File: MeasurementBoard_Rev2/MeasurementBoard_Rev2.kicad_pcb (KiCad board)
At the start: 4 copper layers, 76.2 x 88.9 mm, 113 parts, among them J1 Conn_02x19_Odd_Even, J10 MillMax_0914-2, J19 Conn_01x02_Pin, J2 Conn_02x19_Odd_Even, J20 Conn_01x02_Pin, J21 Conn_01x02_Pin, J22 Conn_01x02_Pin, J3 MillMax_0914-2, J4 MillMax_0914-2, J6 MIllMaxSpringConnector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

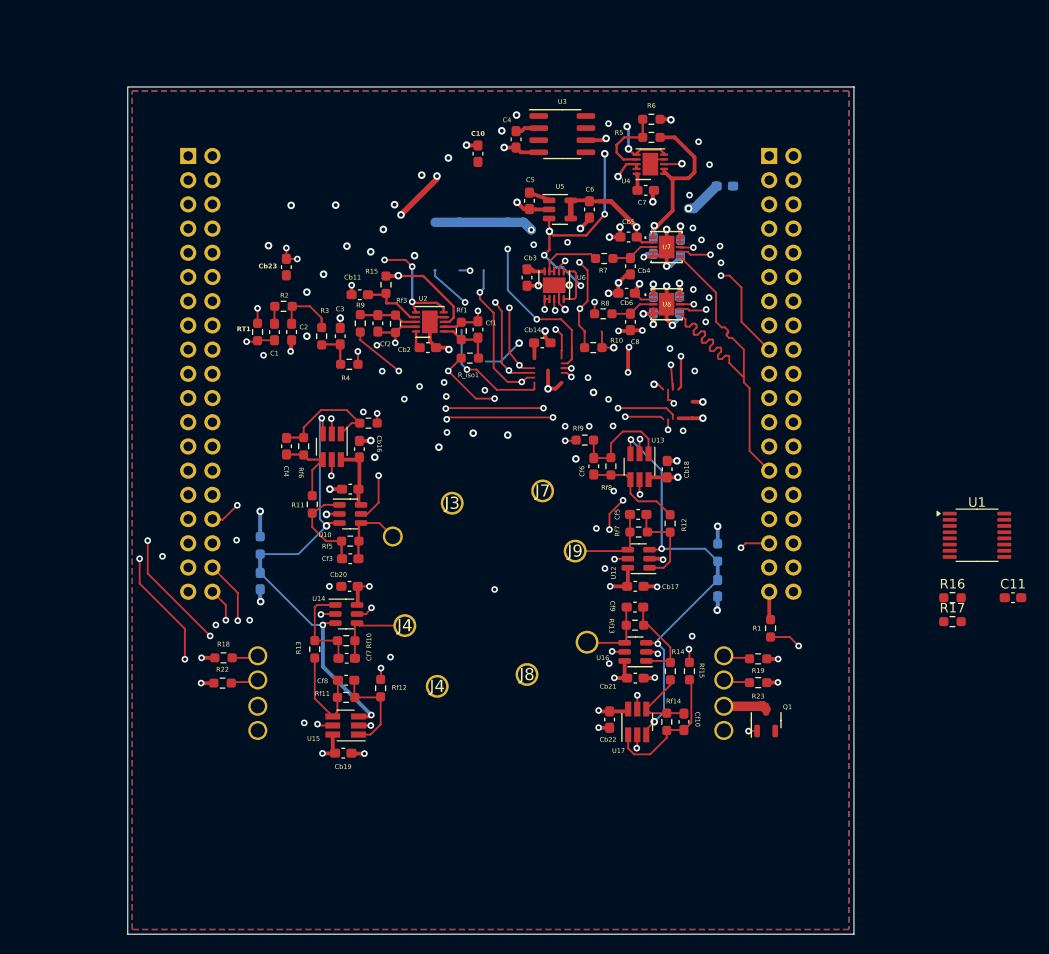
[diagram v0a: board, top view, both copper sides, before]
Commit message: Finished Measurement Board Update Minus Heater Board Connections
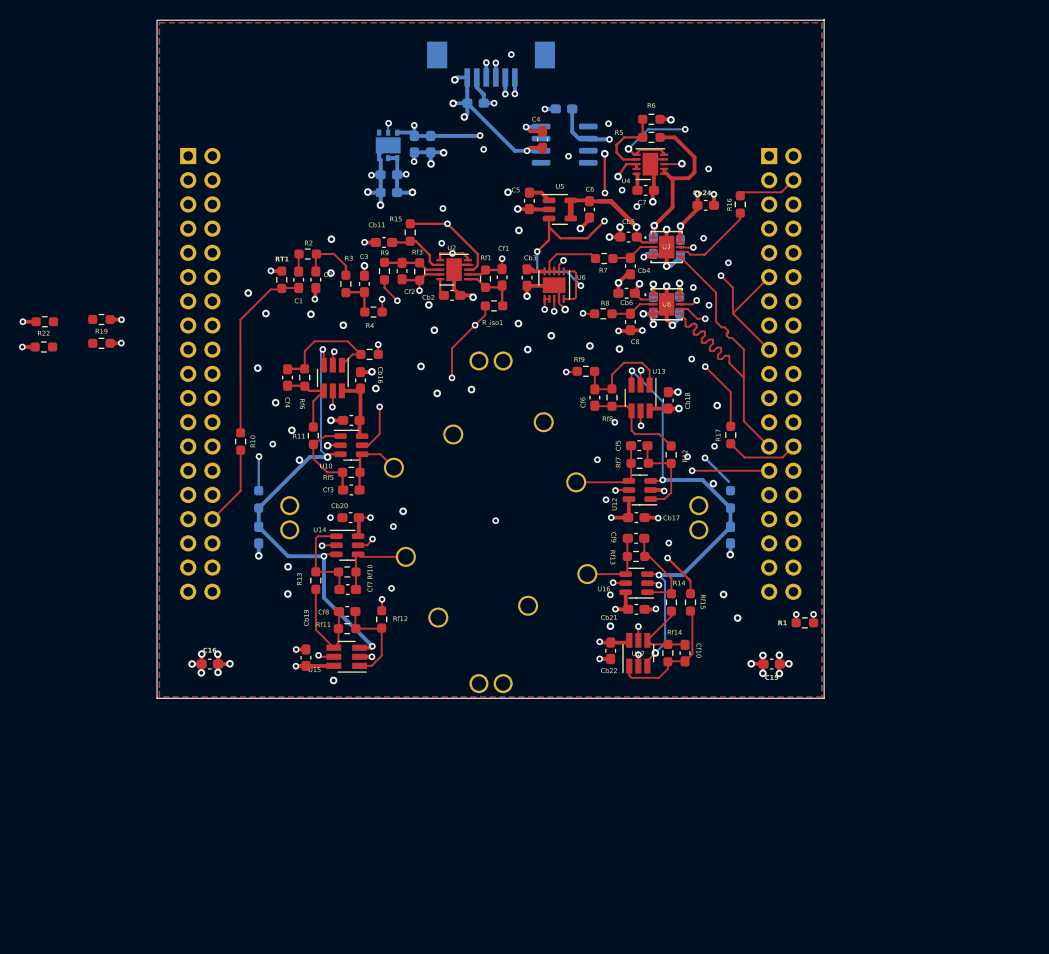
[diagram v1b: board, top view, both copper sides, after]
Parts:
- removed Cb14: 0.1u, Capacitor_SMD:C_0603_1608Metric_Pad1.08x0.95mm_HandSolder
- removed Cb23: 10u, Capacitor_SMD:C_0603_1608Metric_Pad1.08x0.95mm_HandSolder
- removed J10, J9: MillMax_0914-2, 
- removed J19, J20, J21, J22: Conn_01x02_Pin, GenIILibrary:Samtec_Pin_Socket_SS_102_G_2
- removed the J4 at (57.4, 160.9)
- removed the J4 at (54.0, 154.5)
- removed Q1: PMV30UN2, Package_TO_SOT_SMD:SOT-23-3
- removed U1: CD74AC238, Package_SO:TSSOP-16_4.4x5mm_P0.65mm
- added C12: 1uF/XR5, Capacitor_SMD:C_0603_1608Metric_Pad1.08x0.95mm_HandSolder, B.Cu at (52.3, 109.1)
- added C13: 100n, Capacitor_SMD:C_0603_1608Metric_Pad1.08x0.95mm_HandSolder, B.Cu at (55.0, 104.0)
- added C14: 100n, Capacitor_SMD:C_0603_1608Metric_Pad1.08x0.95mm_HandSolder, B.Cu at (52.3, 107.2)
- added C15: 22u, Capacitor_SMD:C_0603_1608Metric_Pad1.08x0.95mm_HandSolder, F.Cu at (92.5, 158.6)
- added C16: 22u, Capacitor_SMD:C_0603_1608Metric_Pad1.08x0.95mm_HandSolder, F.Cu at (33.5, 158.6)
- added C9: 1uF/XR5, Capacitor_SMD:C_0603_1608Metric_Pad1.08x0.95mm_HandSolder, B.Cu at (56.7, 104.0)
- added CN1: Conn_02x19_Odd_Even, Connector_PinSocket_2.54mm:PinSocket_2x19_P2.54mm_Vertical, B.Cu at (31.2, 105.2)
- added CN2: Conn_02x19_Odd_Even, Connector_PinSocket_2.54mm:PinSocket_2x19_P2.54mm_Vertical, B.Cu at (92.2, 105.2)
- added CN3: 52271-0679, GenIILibrary:MOLEX_52271-0679, B.Cu at (63.0, 93.5)
- added CN4: Conn_01x02_Pin, GenIILibrary:Samtec_Pin_Socket_SS_102_G_2, F.Cu at (41.9, 143.2)
- added CN5: Conn_01x02_Pin, GenIILibrary:Samtec_Pin_Socket_SS_102_G_2, F.Cu at (84.8, 143.2)
- added CN6: Conn_01x02_Pin, GenIILibrary:Samtec_Pin_Socket_SS_102_G_2, F.Cu at (63.0, 126.8)
- added CN7: Conn_01x02_Pin, GenIILibrary:Samtec_Pin_Socket_SS_102_G_2, F.Cu at (63.0, 160.6)
- added J4: MIllMaxSpringConnector, TCGenI_Rev3_Redo:MillMax_0914-2, F.Cu at (57.5, 153.7)
- added J5: MIllMaxSpringConnector, TCGenI_Rev3_Redo:MillMax_0914-2, F.Cu at (72.5, 138.1)
- added U9: LD39200_Fixed, Package_DFN_QFN:DFN-6-1EP_3x3mm_P0.95mm_EP1.7x2.6mm, B.Cu at (52.2, 104.1)
- C10, C11, U3: moved to B.Cu
- Cb24: moved to F.Cu
- J1, J2: value Conn_02x19_Odd_Even -> MIllMaxSpringConnector; footprint Connector_PinSocket_2.54mm:PinSocket_2x19_P2.54mm_Vertical -> TCGenI_Rev3_Redo:MillMax_0914-2; moved to F.Cu
- J3, J7, J8: value MillMax_0914-2 -> MIllMaxSpringConnector; footprint (none) -> TCGenI_Rev3_Redo:MillMax_0914-2
- R1: value 10k -> 33
- moved R19 77.6 mm to (22.1, 122.4)
- moved R23 77.6 mm to (22.1, 124.9)
- moved C11 69.6 mm to (70.7, 100.3)
- moved J1 59.6 mm to (73.0, 147.8), turned to 0 degrees
- moved J2 55.2 mm to (55.0, 146.0), turned to 0 degrees
- moved R16 46.9 mm to (89.2, 110.3), turned to 90 degrees
- moved R22 39.9 mm to (16.1, 125.3)
- moved R18 39.9 mm to (16.2, 122.6)
- moved R10 38.3 mm to (36.8, 135.2), turned to 90 degrees
- moved R17 30.4 mm to (88.2, 134.5), turned to 90 degrees
- moved Cb19 10.7 mm to (43.6, 157.9), turned to -90 degrees
- moved J6 9.13 mm to (53.8, 136.1)
- moved J8 8.84 mm to (66.9, 150.8)
- moved Rf9 7.21 mm to (73.0, 127.8)
- moved Cb17 7.21 mm to (78.3, 143.2)
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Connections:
- net /ABBCore_Alt/~{TIA1_SHDN} renamed ~{TIA1_SHDN}
- net /ABBCore_Alt/~{TIA2_SHDN} renamed ~{TIA2_SHDN}
- net /ABBCore_Alt/~{TIA3_SHDN} renamed ~{TIA3_SHDN}
- net /ABBCore_Alt/~{TIA4_SHDN} renamed ~{TIA4_SHDN}
- Cb10 pad 2: Vdd_MCU -> Vdd_Main
- Cb24 pad 2: Vdd_MCU -> Vdd_Main
- Cb9 pad 2: Vdd_MCU -> Vdd_Main
- J1 pad 1: unconnected-(J1-Pin_1-Pad1) -> CCOut_4
- J2 pad 1: unconnected-(J2-Pin_1-Pad1) -> CCOut_3
- R1 pad 1: Net-(Q1-G) -> /MCU Connections/PB6
- R1 pad 2: Heater_PWM -> UART_TX
- R16 pad 2: /MCU Connections/PA6 -> /MCU Connections/PB4
- R17 pad 1: /MCU Connections/PA7 -> /MCU Connections/PB15
- U2 pad 5: ~{CC_Drive_SHDN} -> ~{ADC1_SHDN}
- U2 pad 6: ~{CC_Drive_SHDN} -> ~{ADC1_SHDN}
- U7 pad 10: Vdd_MCU -> Vdd_Main
- U7 pad 9: Vdd_MCU -> Vdd_Main
- U8 pad 10: Vdd_MCU -> Vdd_Main
- U8 pad 9: Vdd_MCU -> Vdd_Main
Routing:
- net /ABBCore_Alt/V_Resp: track 224.5 -> 95.0 mm, vias 19 -> 5
- net UART_TX: track 0.00 -> 92.2 mm, vias 0 -> 2
- net Vdd_MCU: track 72.1 -> 0.00 mm, vias 3 -> 0
- net UART_RX: track 0.00 -> 45.0 mm, vias 0 -> 1
- net ~{CC_Drive_SHDN}: track 34.4 -> 0.00 mm, vias 3 -> 0
- net ~{TIA3_SHDN}: track 65.9 -> 32.1 mm, vias 5 -> 2
- net Vdd_Main: track 48.2 -> 79.8 mm, vias 29 -> 53
- net D1: track 28.3 -> 0.00 mm, vias 2 -> 0
- net D0: track 28.1 -> 0.00 mm, vias 2 -> 0
- net V_MID: track 144.1 -> 117.0 mm, vias 8 -> 4
- net 5V: track 26.9 -> 0.00 mm
- net Heater_EN: track 26.7 -> 1.00 mm, vias 2 -> 1
- net Heater_PG: track 24.6 -> 0.00 mm, vias 2 -> 0
- net Vth_4: track 24.3 -> 0.08 mm
- net ~{TIA4_SHDN}: track 46.9 -> 24.8 mm, vias 3 -> 2
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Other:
- board size 76.2 x 88.9 mm -> 70 x 71.2 mm
- board text added: "Heater"

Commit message: Nearly Finalized Boards
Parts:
- removed R22, R23: 1k, Resistor_SMD:R_0603_1608Metric_Pad0.98x0.95mm_HandSolder
- added R20: 10k, Resistor_SMD:R_0603_1608Metric_Pad0.98x0.95mm_HandSolder, B.Cu at (44.6, 104.3)
- added R21: 10k, Resistor_SMD:R_0603_1608Metric_Pad0.98x0.95mm_HandSolder, B.Cu at (44.6, 106.1)
- CN3: value 52271-0679 -> 522070860; footprint GenIILibrary:MOLEX_52271-0679 -> GenIILibrary:CON_522070860_MOL
- moved R19 69.1 mm to (86.1, 148.7), turned to 90 degrees
- moved R18 36.0 mm to (40.3, 149.4), turned to 90 degrees
- moved CN7 33.9 mm to (63.0, 126.7)
- moved CN6 33.5 mm to (63.0, 160.2), turned to -90 degrees
- moved C10 5.48 mm to (65.4, 103.4), turned to -90 degrees
- moved Cb19 5.02 mm to (47.8, 160.6), turned to 180 degrees
- moved CN3 1.30 mm to (63.0, 94.8)
- moved CN5 1.11 mm to (83.8, 143.5)
- moved CN4 0.45 mm to (42.2, 143.5)
- moved R10 0.16 mm to (36.9, 135.2)
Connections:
- C12 pad 1: /Power and References/Vdd_Heater -> /Heater_Interface/Heater+
- C14 pad 1: /Power and References/Vdd_Heater -> /Heater_Interface/Heater+
- CN1 pad 2: unconnected-(CN1-Pin_2-Pad2) -> ~{CHARGE_EN}
- CN1 pad 38: Vth_3 -> /MCU Connections/PC2
- CN1 pad 4: unconnected-(CN1-Pin_4-Pad4) -> /MCU Connections/PE4
- CN2 pad 29: Vth_4 -> /MCU Connections/PC10
- CN3 pad 1: Vdd_Main -> V_Batt
- CN3 pad 2: GND -> ~{CHARGE_EN}
- CN3 pad 3: UART_TX -> Vcc
- CN3 pad 4: UART_RX -> GND
- CN3 pad 5: GND -> UART_RX
- CN3 pad 6: Vcc -> UART_TX
- CN4 pad 1: Heater+ -> Vdd_Main
- CN4 pad 2: unconnected-(CN4-Pin_2-Pad2) -> Vth_1
- CN5 pad 1: Vth_1 -> Vdd_Main
- CN5 pad 2: Vth_3 -> Vth_2
- CN6 pad 1: Heater- -> unconnected-(CN6-Pin_1-Pad1)
- CN7 pad 1: Vth_2 -> GND
- CN7 pad 2: Vth_4 -> /Heater_Interface/Heater+
- U9 pad 1: /Power and References/Vdd_Heater -> /Heater_Interface/Heater+
- U9 pad 2: /Power and References/Vdd_Heater -> /Heater_Interface/Heater+
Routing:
- net /MCU Connections/PC1: track 0.00 -> 41.2 mm, vias 0 -> 2
- net ~{CHARGE_EN}: track 0.00 -> 32.4 mm, vias 0 -> 2
- net /Heater_Interface/Heater+: track 0.00 -> 29.4 mm, vias 0 -> 2
- net Heater_EN: track 1.00 -> 23.4 mm
- net GND: track 118.7 -> 138.5 mm, vias 84 -> 101
- net Vth_2: track 0.14 -> 19.9 mm, vias 0 -> 1
- net V_Batt: track 0.00 -> 16.7 mm
- net Vth_1: track 0.00 -> 11.8 mm, vias 0 -> 1
- net Vdd_Main: track 79.8 -> 71.2 mm, vias 53 -> 66
- net /Power and References/Vdd_Heater: track 7.19 -> 0.00 mm, vias 2 -> 0
- net ~{TIA3_SHDN}: track 32.1 -> 35.7 mm
- net Vcc: track 17.6 -> 14.2 mm, vias 3 -> 1
- net ~{ADC1_SHDN}: track 68.1 -> 69.9 mm, vias 8 -> 7
- net V_MID: track 117.0 -> 118.0 mm
- net UART_RX: track 45.0 -> 45.7 mm
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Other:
- board text removed: "Heater"

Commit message: Final commit before order
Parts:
- RT1: value 0 -> NC
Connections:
- CN2 pad 33: Vth_2 -> ~{TIA4_SHDN}
- CN2 pad 35: ~{TIA4_SHDN} -> Vth_2
- CN3 pad 5: UART_RX -> UART_TX
- CN3 pad 6: UART_TX -> UART_RX
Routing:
- net Vth_2: track 19.9 -> 10.4 mm
- net ~{ADC1_SHDN}: track 69.9 -> 65.3 mm, vias 7 -> 5
- net Vdd_Main: track 71.2 -> 67.8 mm, vias 66 -> 75
- net /Heater_Interface/Heater+: track 29.4 -> 32.5 mm
- net ~{TIA4_SHDN}: track 24.8 -> 27.4 mm
- net Vcc: track 14.2 -> 12.1 mm, vias 1 -> 2
- net /ABBCore_Alt/V_Resp: track 95.4 -> 94.0 mm
- net GND: track 138.5 -> 139.6 mm, vias 101 -> 117
- net UART_RX: track 45.7 -> 44.8 mm
- net /ABBCore_Alt/V_Drive: track 89.2 -> 89.8 mm, vias 4 -> 5
- net V_Batt: vias 0 -> 2
- net Net-(U6A--): vias 2 -> 0
- net /ABBCore_Alt/TIA_1/V_MID: vias 4 -> 6
- net /ABBCore_Alt/TIA_2/V_MID: vias 4 -> 6
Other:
- outline, holes or cut-outs redrawn
